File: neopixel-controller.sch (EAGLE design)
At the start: 13 parts, among them J1 Power, J2 AVR_SPI_PROG_3X2NS, U1 ATTiny85

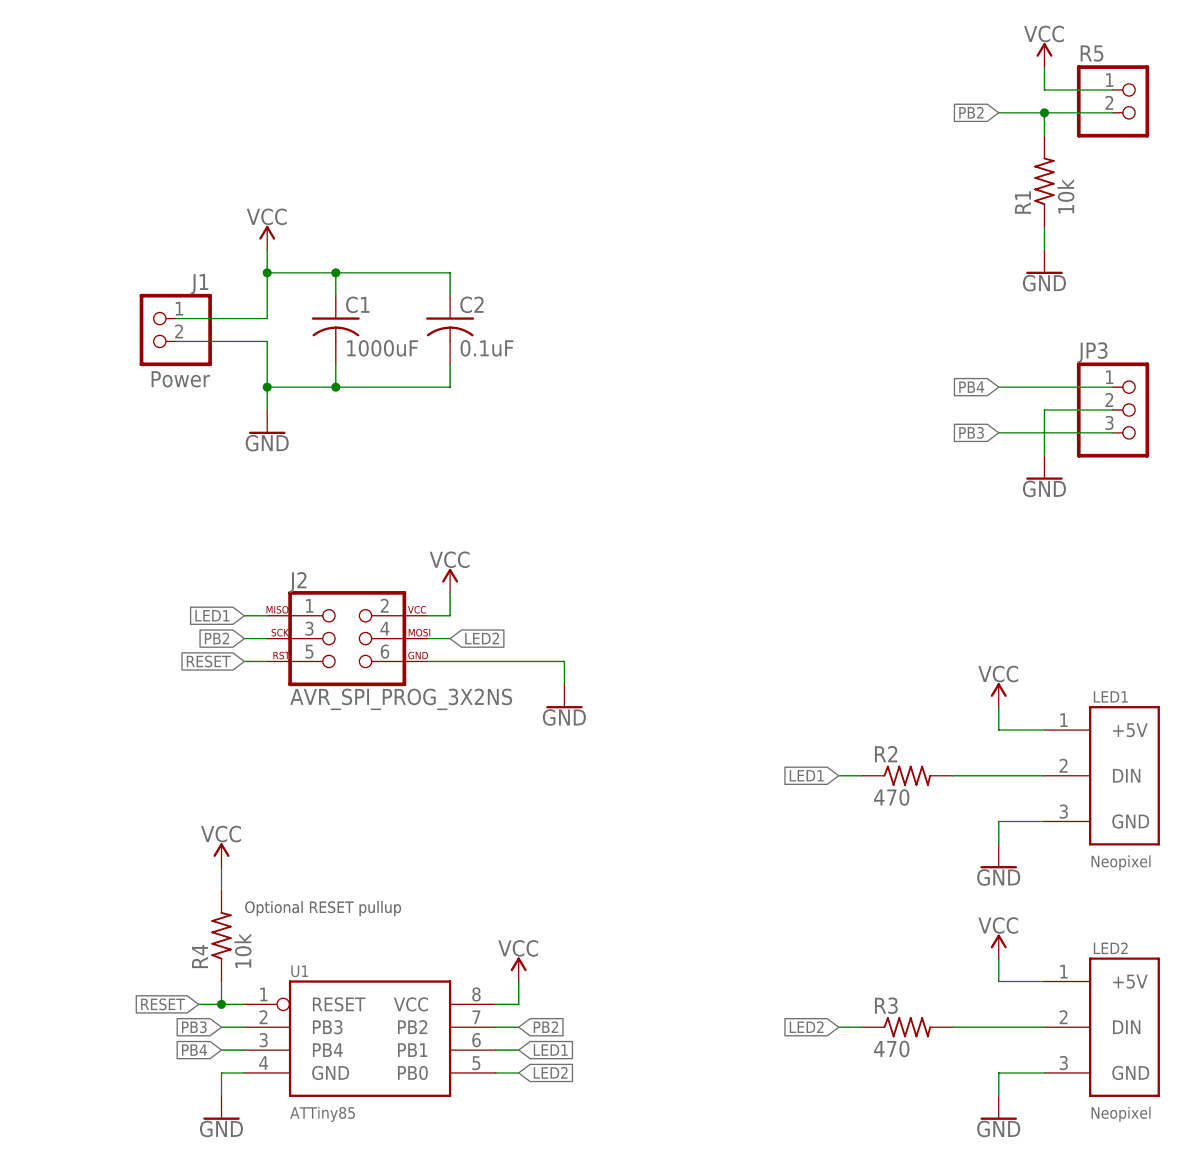
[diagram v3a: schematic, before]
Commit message: Initial redesign for production run 2
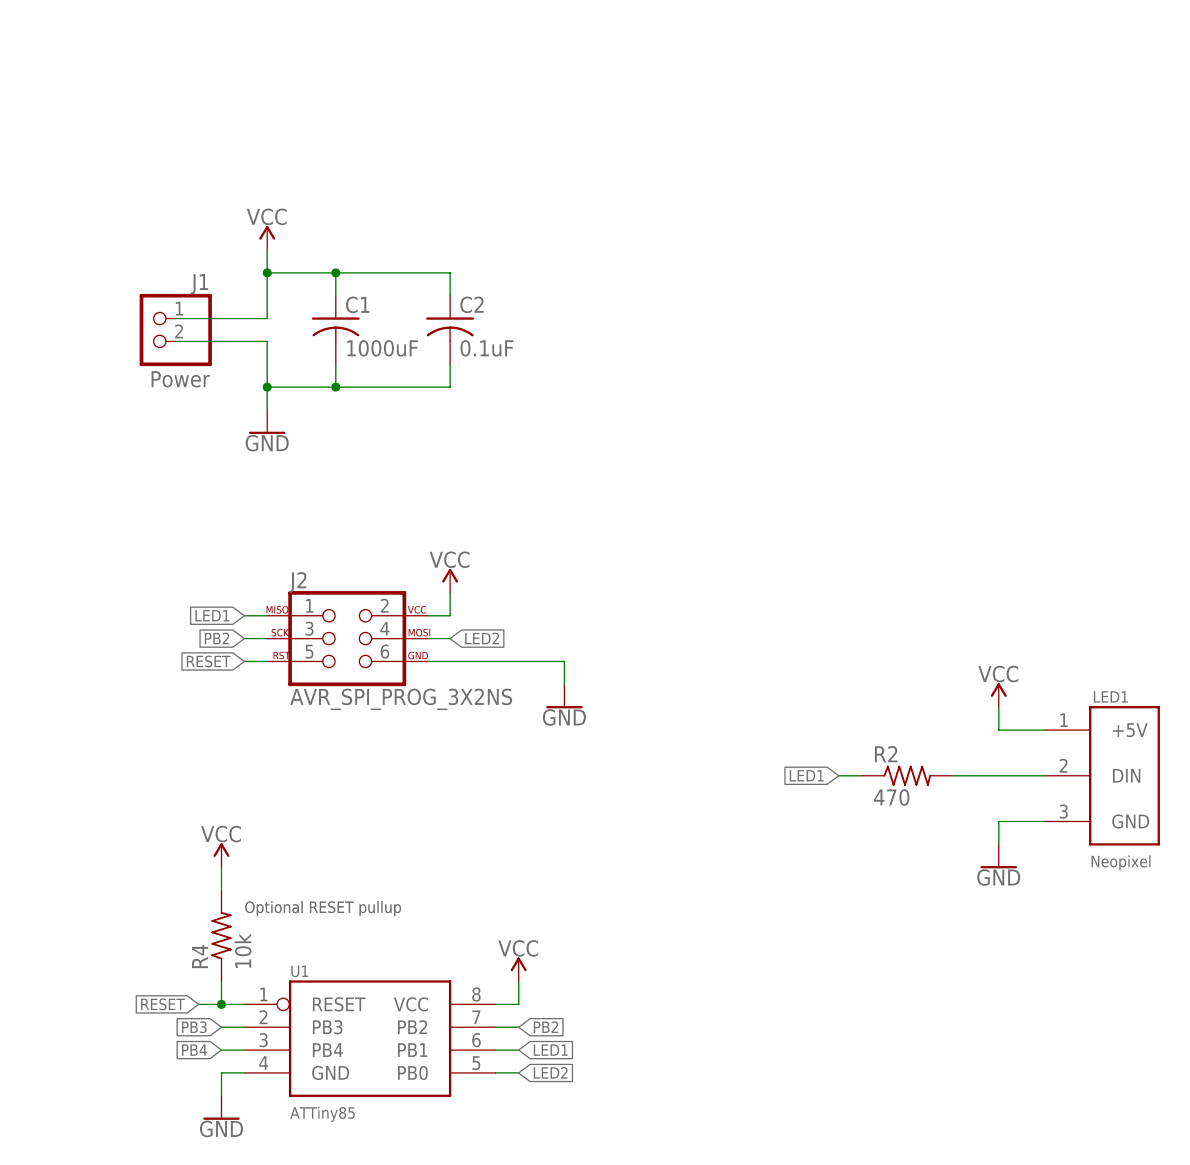
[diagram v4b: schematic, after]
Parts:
- removed JP3: (no value), pinhead:PINHD-1X3
- removed LED2: Neopixel, JoshCustom:NEOPIXEL0.100_PINHEAD
- removed R1: 10k, resistor:R-US_R0805
- removed R3: 470, resistor:R-US_R0805
- removed R5: (no value), pinhead:PINHD-1X2
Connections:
- removed net N$1: LED2.DIN, R3.2
- net GND: no longer JP3.2, LED2.GND, R1.1
- net LED2: no longer R3.1
- net PB2: no longer R1.2, R5.2
- net PB3: no longer JP3.3
- net PB4: no longer JP3.1
- net VCC: no longer LED2.+5V, R5.1
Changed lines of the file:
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@@
 <part name="U1" library="JoshCustom" deviceset="ATTINY85" device="SOIC8" value="ATTiny85"/>
 <part name="LED1" library="JoshCustom" deviceset="NEOPIXEL" device="0.100_PINHEAD" value="Neopixel"/>
-<part name="LED2" library="JoshCustom" deviceset="NEOPIXEL" device="0.100_PINHEAD" value="Neopixel"/>
-<part name="R5" library="pinhead" library_urn="urn:adsk.eagle:library:325" deviceset="PINHD-1X2" device="" package3d_urn="urn:adsk.eagle:package:22435/2"/>
-<part name="R1" library="resistor" library_urn="urn:adsk.eagle:library:348" deviceset="R-US_" device="R0805" package3d_urn="urn:adsk.eagle:package:26059/1" value="10k"/>
 <part name="R2" library="resistor" library_urn="urn:adsk.eagle:library:348" deviceset="R-US_" device="R0805" package3d_urn="urn:adsk.eagle:package:26059/1" value="470"/>
-<part name="R3" library="resistor" library_urn="urn:adsk.eagle:library:348" deviceset="R-US_" device="R0805" package3d_urn="urn:adsk.eagle:package:26059/1" value="470"/>
 <part name="R4" library="resistor" library_urn="urn:adsk.eagle:library:348" deviceset="R-US_" device="R0805" package3d_urn="urn:adsk.eagle:package:26059/1" value="10k"/>
 <part name="SUPPLY1" library="SparkFun-PowerSymbols" deviceset="VCC" device=""/>
 <part name="SUPPLY2" library="SparkFun-PowerSymbols" deviceset="VCC" device=""/>
-<part name="SUPPLY3" library="SparkFun-PowerSymbols" deviceset="VCC" device=""/>
 <part name="SUPPLY4" library="SparkFun-PowerSymbols" deviceset="VCC" device=""/>
 <part name="GND1" library="SparkFun-PowerSymbols" deviceset="GND" device=""/>
 <part name="GND2" library="SparkFun-PowerSymbols" deviceset="GND" device=""/>
 <part name="GND3" library="SparkFun-PowerSymbols" deviceset="GND" device=""/>
-<part name="GND4" library="SparkFun-PowerSymbols" deviceset="GND" device=""/>
 <part name="SUPPLY5" library="SparkFun-PowerSymbols" deviceset="VCC" device=""/>
-<part name="GND5" library="SparkFun-PowerSymbols" deviceset="GND" device=""/>
-<part name="GND6" library="SparkFun-PowerSymbols" deviceset="GND" device=""/>
-<part name="SUPPLY7" library="SparkFun-PowerSymbols" deviceset="VCC" device=""/>
 <part name="C2" library="resistor" library_urn="urn:adsk.eagle:library:348" deviceset="C-US" device="C0805" package3d_urn="urn:adsk.eagle:package:23617/2" value="0.1uF"/>
 <part name="C1" library="JoshCustom" deviceset="CAPACITOR" device="" value="1000uF"/>
@@
 <part name="SUPPLY6" library="SparkFun-PowerSymbols" deviceset="VCC" device=""/>
 <part name="GND7" library="SparkFun-PowerSymbols" deviceset="GND" device=""/>
-<part name="JP3" library="pinhead" library_urn="urn:adsk.eagle:library:325" deviceset="PINHD-1X3" device="" package3d_urn="urn:adsk.eagle:package:22458/2"/>
 </parts>
 <sheets>
@@
 <attribute name="VALUE" x="109.22" y="30.48" size="1.27" layer="96"/>
 </instance>
-<instance part="LED2" gate="G$1" x="109.22" y="5.08" smashed="yes">
-<attribute name="NAME" x="109.474" y="20.828" size="1.27" layer="95"/>
-<attribute name="VALUE" x="109.22" y="2.54" size="1.27" layer="96"/>
-</instance>
-<instance part="R5" gate="G$1" x="114.3" y="114.3" smashed="yes">
-<attribute name="NAME" x="107.95" y="120.015" size="1.778" layer="95"/>
-<attribute name="VALUE" x="107.95" y="109.22" size="1.778" layer="96"/>
-</instance>
-<instance part="R1" gate="G$1" x="104.14" y="106.68" smashed="yes" rot="R90">
-<attribute name="NAME" x="102.6414" y="102.87" size="1.778" layer="95" rot="R90"/>
-<attribute name="VALUE" x="107.442" y="102.87" size="1.778" layer="96" rot="R90"/>
-</instance>
 <instance part="R2" gate="G$1" x="88.9" y="40.64" smashed="yes">
 <attribute name="NAME" x="85.09" y="42.1386" size="1.778" layer="95"/>
 <attribute name="VALUE" x="85.09" y="37.338" size="1.778" layer="96"/>
 </instance>
-<instance part="R3" gate="G$1" x="88.9" y="12.7" smashed="yes">
-<attribute name="NAME" x="85.09" y="14.1986" size="1.778" layer="95"/>
-<attribute name="VALUE" x="85.09" y="9.398" size="1.778" layer="96"/>
-</instance>
 <instance part="R4" gate="G$1" x="12.7" y="22.86" smashed="yes" rot="R90">
 <attribute name="NAME" x="11.2014" y="19.05" size="1.778" layer="95" rot="R90"/>
@@
 <attribute name="VALUE" x="45.72" y="20.574" size="1.778" layer="96" align="bottom-center"/>
 </instance>
-<instance part="SUPPLY3" gate="G$1" x="99.06" y="20.32" smashed="yes">
-<attribute name="VALUE" x="99.06" y="23.114" size="1.778" layer="96" align="bottom-center"/>
-</instance>
 <instance part="SUPPLY4" gate="G$1" x="99.06" y="48.26" smashed="yes">
 <attribute name="VALUE" x="99.06" y="51.054" size="1.778" layer="96" align="bottom-center"/>
@@
 <attribute name="VALUE" x="99.06" y="30.226" size="1.778" layer="96" align="top-center"/>
 </instance>
-<instance part="GND4" gate="1" x="99.06" y="2.54" smashed="yes">
-<attribute name="VALUE" x="99.06" y="2.286" size="1.778" layer="96" align="top-center"/>
-</instance>
 <instance part="SUPPLY5" gate="G$1" x="12.7" y="30.48" smashed="yes">
 <attribute name="VALUE" x="12.7" y="33.274" size="1.778" layer="96" align="bottom-center"/>
-</instance>
-<instance part="GND5" gate="1" x="104.14" y="73.66" smashed="yes">
-<attribute name="VALUE" x="104.14" y="73.406" size="1.778" layer="96" align="top-center"/>
-</instance>
-<instance part="GND6" gate="1" x="104.14" y="96.52" smashed="yes">
-<attribute name="VALUE" x="104.14" y="96.266" size="1.778" layer="96" align="top-center"/>
-</instance>
-<instance part="SUPPLY7" gate="G$1" x="104.14" y="119.38" smashed="yes">
-<attribute name="VALUE" x="104.14" y="122.174" size="1.778" layer="96" align="bottom-center"/>
 </instance>
 <instance part="C2" gate="G$1" x="38.1" y="91.44" smashed="yes">
@@
 <instance part="GND7" gate="1" x="50.8" y="48.26" smashed="yes">
 <attribute name="VALUE" x="50.8" y="48.006" size="1.778" layer="96" align="top-center"/>
-</instance>
-<instance part="JP3" gate="A" x="114.3" y="81.28" smashed="yes">
-<attribute name="NAME" x="107.95" y="86.995" size="1.778" layer="95"/>
-<attribute name="VALUE" x="107.95" y="73.66" size="1.778" layer="96"/>
 </instance>
 </instances>
@@
 </segment>
 <segment>
-<pinref part="LED2" gate="G$1" pin="+5V"/>
-<wire x1="104.14" y1="17.78" x2="99.06" y2="17.78" width="0.1524" layer="91"/>
-<pinref part="SUPPLY3" gate="G$1" pin="VCC"/>
-<wire x1="99.06" y1="17.78" x2="99.06" y2="20.32" width="0.1524" layer="91"/>
-</segment>
-<segment>
 <pinref part="LED1" gate="G$1" pin="+5V"/>
 <wire x1="104.14" y1="45.72" x2="99.06" y2="45.72" width="0.1524" layer="91"/>
@@
 <pinref part="SUPPLY5" gate="G$1" pin="VCC"/>
 <wire x1="12.7" y1="27.94" x2="12.7" y2="30.48" width="0.1524" layer="91"/>
-</segment>
-<segment>
-<pinref part="R5" gate="G$1" pin="1"/>
-<pinref part="SUPPLY7" gate="G$1" pin="VCC"/>
-<wire x1="111.76" y1="116.84" x2="104.14" y2="116.84" width="0.1524" layer="91"/>
-<wire x1="104.14" y1="116.84" x2="104.14" y2="119.38" width="0.1524" layer="91"/>
 </segment>
 <segment>
@@
 </segment>
 <segment>
-<pinref part="GND4" gate="1" pin="GND"/>
-<wire x1="99.06" y1="5.08" x2="99.06" y2="7.62" width="0.1524" layer="91"/>
-<pinref part="LED2" gate="G$1" pin="GND"/>
-<wire x1="99.06" y1="7.62" x2="104.14" y2="7.62" width="0.1524" layer="91"/>
-</segment>
-<segment>
 <pinref part="GND3" gate="1" pin="GND"/>
 <wire x1="99.06" y1="33.02" x2="99.06" y2="35.56" width="0.1524" layer="91"/>
@@
 </segment>
 <segment>
-<pinref part="R1" gate="G$1" pin="1"/>
-<pinref part="GND6" gate="1" pin="GND"/>
-<wire x1="104.14" y1="101.6" x2="104.14" y2="99.06" width="0.1524" layer="91"/>
-</segment>
-<segment>
-<pinref part="GND5" gate="1" pin="GND"/>
-<wire x1="111.76" y1="81.28" x2="104.14" y2="81.28" width="0.1524" layer="91"/>
-<wire x1="104.14" y1="81.28" x2="104.14" y2="76.2" width="0.1524" layer="91"/>
-<pinref part="JP3" gate="A" pin="2"/>
-</segment>
-<segment>
 <pinref part="J2" gate="G$1" pin="6"/>
 <wire x1="35.56" y1="53.34" x2="50.8" y2="53.34" width="0.1524" layer="91"/>
@@
 </segment>
 </net>
-<net name="N$1" class="0">
-<segment>
-<pinref part="LED2" gate="G$1" pin="DIN"/>
-<pinref part="R3" gate="G$1" pin="2"/>
-<wire x1="104.14" y1="12.7" x2="93.98" y2="12.7" width="0.1524" layer="91"/>
-</segment>
-</net>
 <net name="N$2" class="0">
 <segment>
@@
 <label x="12.7" y="12.7" size="1.27" layer="95" rot="R180" xref="yes"/>
 </segment>
-<segment>
-<wire x1="111.76" y1="78.74" x2="99.06" y2="78.74" width="0.1524" layer="91"/>
-<label x="99.06" y="78.74" size="1.27" layer="95" rot="R180" xref="yes"/>
-<pinref part="JP3" gate="A" pin="3"/>
-</segment>
 </net>
 <net name="PB4" class="0">
@@
 <label x="12.7" y="10.16" size="1.27" layer="95" rot="R180" xref="yes"/>
 </segment>
-<segment>
-<wire x1="111.76" y1="83.82" x2="99.06" y2="83.82" width="0.1524" layer="91"/>
-<label x="99.06" y="83.82" size="1.27" layer="95" rot="R180" xref="yes"/>
-<pinref part="JP3" gate="A" pin="1"/>
-</segment>
 </net>
 <net name="PB2" class="0">
@@
 </segment>
 <segment>
-<pinref part="R5" gate="G$1" pin="2"/>
-<pinref part="R1" gate="G$1" pin="2"/>
-<wire x1="111.76" y1="114.3" x2="104.14" y2="114.3" width="0.1524" layer="91"/>
-<wire x1="104.14" y1="114.3" x2="104.14" y2="111.76" width="0.1524" layer="91"/>
-<wire x1="104.14" y1="114.3" x2="99.06" y2="114.3" width="0.1524" layer="91"/>
-<junction x="104.14" y="114.3"/>
-<label x="99.06" y="114.3" size="1.27" layer="95" rot="R180" xref="yes"/>
-</segment>
-<segment>
 <pinref part="J2" gate="G$1" pin="3"/>
 <wire x1="17.78" y1="55.88" x2="15.24" y2="55.88" width="0.1524" layer="91"/>
@@
 </segment>
 <segment>
-<pinref part="R3" gate="G$1" pin="1"/>
-<wire x1="83.82" y1="12.7" x2="81.28" y2="12.7" width="0.1524" layer="91"/>
-<label x="81.28" y="12.7" size="1.27" layer="95" rot="R180" xref="yes"/>
-</segment>
-<segment>
